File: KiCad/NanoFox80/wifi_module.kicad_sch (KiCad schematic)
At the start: 8 parts, among them U201 TPS22810DBVT, U202 74HC1G08

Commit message: Development
o Set all footprints to approximate values
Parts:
- C201: value 10uF -> (none); footprint Capacitors_SMD:C_0805 -> (none)
- C202: value 4.7uF -> (none); footprint Capacitors_SMD:C_0805 -> (none)
- C203: value 100nF -> (none); footprint Capacitors_SMD:C_0805 -> (none)
- MOD201: value HUZZAH_ESP8266_Breakout -> (none); footprint Oddities:Adafruit_HUZZAH_ESP8266_Breakout_SM -> (none)
- R201: value 560k -> (none); footprint Resistors_SMD:R_0805 -> (none)
- R202: value 10k -> (none); footprint Resistors_SMD:R_0805 -> (none)
- U201: value TPS22810DBVT -> (none); footprint TO_SOT_Packages_SMD:SOT-23-6 -> (none)
- U202: value 74HC1G08 -> (none); footprint TO_SOT_Packages_SMD:SOT-23-5 -> (none)
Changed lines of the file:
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@@
     (in_bom yes) (on_board yes)
     (property "Reference" "R202" (id 0) (at 220.98 99.822 90))
-    (property "Value" "10k" (id 1) (at 220.98 97.79 90))
-    (property "Footprint" "Resistors_SMD:R_0805" (id 2) (at 220.98 96.012 0)
+    (property "Value" "" (id 1) (at 220.98 97.79 90))
+    (property "Footprint" "" (id 2) (at 220.98 96.012 0)
       (effects (font (size 1.27 1.27)) hide)
     )
@@
       (effects (font (size 1.5494 1.5494) bold))
     )
-    (property "Value" "74HC1G08" (id 1) (at 135.89 110.49 0)
+    (property "Value" "" (id 1) (at 135.89 110.49 0)
       (effects (font (size 1.5494 1.5494) bold))
     )
-    (property "Footprint" "TO_SOT_Packages_SMD:SOT-23-5" (id 2) (at 134.62 109.22 0)
+    (property "Footprint" "" (id 2) (at 134.62 109.22 0)
       (effects (font (size 1.27 1.27)) hide)
     )
@@
       (effects (font (size 1.27 1.27)) (justify left))
     )
-    (property "Value" "4.7uF" (id 1) (at 247.015 88.9 0)
-      (effects (font (size 1.27 1.27)) (justify left))
-    )
-    (property "Footprint" "Capacitors_SMD:C_0805" (id 2) (at 247.3452 87.63 0)
+    (property "Value" "" (id 1) (at 247.015 88.9 0)
+      (effects (font (size 1.27 1.27)) (justify left))
+    )
+    (property "Footprint" "" (id 2) (at 247.3452 87.63 0)
       (effects (font (size 1.27 1.27)) hide)
     )
@@
       (effects (font (size 1.5494 1.5494) bold))
     )
-    (property "Value" "TPS22810DBVT" (id 1) (at 228.6 82.5759 0)
+    (property "Value" "" (id 1) (at 228.6 82.5759 0)
       (effects (font (size 1.5494 1.5494) bold))
     )
-    (property "Footprint" "TO_SOT_Packages_SMD:SOT-23-6" (id 2) (at 228.6 106.68 0)
+    (property "Footprint" "" (id 2) (at 228.6 106.68 0)
       (effects (font (size 1.27 1.27)) hide)
     )
@@
       (effects (font (size 1.27 1.27) bold))
     )
-    (property "Value" "HUZZAH_ESP8266_Breakout" (id 1) (at 177.8 109.22 0)
+    (property "Value" "" (id 1) (at 177.8 109.22 0)
       (effects (font (size 1.27 1.27) bold))
     )
-    (property "Footprint" "Oddities:Adafruit_HUZZAH_ESP8266_Breakout_SM" (id 2) (at 177.8 95.25 0)
+    (property "Footprint" "" (id 2) (at 177.8 95.25 0)
       (effects (font (size 1.27 1.27)) hide)
     )
@@
     (in_bom yes) (on_board yes)
     (property "Reference" "R201" (id 0) (at 117.602 95.25 90))
-    (property "Value" "560k" (id 1) (at 115.57 95.25 90))
-    (property "Footprint" "Resistors_SMD:R_0805" (id 2) (at 113.792 95.25 0)
+    (property "Value" "" (id 1) (at 115.57 95.25 90))
+    (property "Footprint" "" (id 2) (at 113.792 95.25 0)
       (effects (font (size 1.27 1.27)) hide)
     )
@@
       (effects (font (size 1.27 1.27)) (justify left))
     )
-    (property "Value" "10uF" (id 1) (at 210.185 88.9 0)
-      (effects (font (size 1.27 1.27)) (justify left))
-    )
-    (property "Footprint" "Capacitors_SMD:C_0805" (id 2) (at 210.5152 87.63 0)
+    (property "Value" "" (id 1) (at 210.185 88.9 0)
+      (effects (font (size 1.27 1.27)) (justify left))
+    )
+    (property "Footprint" "" (id 2) (at 210.5152 87.63 0)
       (effects (font (size 1.27 1.27)) hide)
     )
@@
       (effects (font (size 1.27 1.27)) (justify left))
     )
-    (property "Value" "100nF" (id 1) (at 137.16 102.87 90)
-      (effects (font (size 1.27 1.27)) (justify left))
-    )
-    (property "Footprint" "Capacitors_SMD:C_0805" (id 2) (at 134.62 100.33 0)
-      (effects (font (size 1.27 1.27)) hide)
-    )
+    (property "Value" "" (id 1) (at 137.16 102.87 90)
+      (effects (font (size 1.27 1.27)) (justify left))
+    )
+    (property "Footprint" "" (id 2) (at 134.62 100.33 0)
+      (effects (font (size 1.27 1.27)) hide)
+    )

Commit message: Development
o Updated version and date information
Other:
- title: (none) -> NanoFox80 Foxoring Transmitter
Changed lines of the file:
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@@
 (kicad_sch (version 20211123) (generator eeschema)
   (paper "A4")
+  (title_block
+    (title "NanoFox80 Foxoring Transmitter")
+    (date "2022-07-01")
+    (rev "0.4")
+  )
   (junction (at 209.55 86.36) (diameter 0) (color 0 0 0 0)
   )

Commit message: Development
o Changes to footprints in schematic
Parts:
- C201: value (none) -> 10uF; footprint (none) -> Capacitor_SMD:C_0805_2012Metric
- C202: value (none) -> 4.7uF; footprint (none) -> Capacitor_SMD:C_0805_2012Metric
- C203: value (none) -> 100nF; footprint (none) -> Capacitor_SMD:C_0805_2012Metric
- MOD201: value (none) -> HUZZAH_ESP8266_Breakout; footprint (none) -> Oddities:Adafruit_HUZZAH_ESP8266_Breakout_SM
- R201: value (none) -> 560k; footprint (none) -> Resistor_SMD:R_0805_2012Metric
- R202: value (none) -> 10k; footprint (none) -> Resistor_SMD:R_0805_2012Metric
- U201: value (none) -> TPS22810DBVT; footprint (none) -> Package_TO_SOT_SMD:SOT-23-6
- U202: value (none) -> 74HC1G08; footprint (none) -> Package_TO_SOT_SMD:SOT-23-5
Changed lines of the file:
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@@
     (in_bom yes) (on_board yes)
     (property "Reference" "R202" (id 0) (at 220.98 99.822 90))
-    (property "Value" "" (id 1) (at 220.98 97.79 90))
-    (property "Footprint" "" (id 2) (at 220.98 96.012 0)
+    (property "Value" "10k" (id 1) (at 220.98 97.79 90))
+    (property "Footprint" "Resistor_SMD:R_0805_2012Metric" (id 2) (at 220.98 96.012 0)
       (effects (font (size 1.27 1.27)) hide)
     )
@@
       (effects (font (size 1.5494 1.5494) bold))
     )
-    (property "Value" "" (id 1) (at 135.89 110.49 0)
+    (property "Value" "74HC1G08" (id 1) (at 135.89 110.49 0)
       (effects (font (size 1.5494 1.5494) bold))
     )
-    (property "Footprint" "" (id 2) (at 134.62 109.22 0)
+    (property "Footprint" "Package_TO_SOT_SMD:SOT-23-5" (id 2) (at 134.62 109.22 0)
       (effects (font (size 1.27 1.27)) hide)
     )
@@
       (effects (font (size 1.27 1.27)) (justify left))
     )
-    (property "Value" "" (id 1) (at 247.015 88.9 0)
-      (effects (font (size 1.27 1.27)) (justify left))
-    )
-    (property "Footprint" "" (id 2) (at 247.3452 87.63 0)
+    (property "Value" "4.7uF" (id 1) (at 247.015 88.9 0)
+      (effects (font (size 1.27 1.27)) (justify left))
+    )
+    (property "Footprint" "Capacitor_SMD:C_0805_2012Metric" (id 2) (at 247.3452 87.63 0)
       (effects (font (size 1.27 1.27)) hide)
     )
@@
       (effects (font (size 1.5494 1.5494) bold))
     )
-    (property "Value" "" (id 1) (at 228.6 82.5759 0)
+    (property "Value" "TPS22810DBVT" (id 1) (at 228.6 82.5759 0)
       (effects (font (size 1.5494 1.5494) bold))
     )
-    (property "Footprint" "" (id 2) (at 228.6 106.68 0)
+    (property "Footprint" "Package_TO_SOT_SMD:SOT-23-6" (id 2) (at 228.6 106.68 0)
       (effects (font (size 1.27 1.27)) hide)
     )
@@
       (effects (font (size 1.27 1.27) bold))
     )
-    (property "Value" "" (id 1) (at 177.8 109.22 0)
+    (property "Value" "HUZZAH_ESP8266_Breakout" (id 1) (at 177.8 109.22 0)
       (effects (font (size 1.27 1.27) bold))
     )
-    (property "Footprint" "" (id 2) (at 177.8 95.25 0)
+    (property "Footprint" "Oddities:Adafruit_HUZZAH_ESP8266_Breakout_SM" (id 2) (at 177.8 95.25 0)
       (effects (font (size 1.27 1.27)) hide)
     )
@@
     (in_bom yes) (on_board yes)
     (property "Reference" "R201" (id 0) (at 117.602 95.25 90))
-    (property "Value" "" (id 1) (at 115.57 95.25 90))
-    (property "Footprint" "" (id 2) (at 113.792 95.25 0)
+    (property "Value" "560k" (id 1) (at 115.57 95.25 90))
+    (property "Footprint" "Resistor_SMD:R_0805_2012Metric" (id 2) (at 113.792 95.25 0)
       (effects (font (size 1.27 1.27)) hide)
     )
@@
       (effects (font (size 1.27 1.27)) (justify left))
     )
-    (property "Value" "" (id 1) (at 210.185 88.9 0)
-      (effects (font (size 1.27 1.27)) (justify left))
-    )
-    (property "Footprint" "" (id 2) (at 210.5152 87.63 0)
+    (property "Value" "10uF" (id 1) (at 210.185 88.9 0)
+      (effects (font (size 1.27 1.27)) (justify left))
+    )
+    (property "Footprint" "Capacitor_SMD:C_0805_2012Metric" (id 2) (at 210.5152 87.63 0)
       (effects (font (size 1.27 1.27)) hide)
     )
@@
       (effects (font (size 1.27 1.27)) (justify left))
     )
-    (property "Value" "" (id 1) (at 137.16 102.87 90)
-      (effects (font (size 1.27 1.27)) (justify left))
-    )
-    (property "Footprint" "" (id 2) (at 134.62 100.33 0)
-      (effects (font (size 1.27 1.27)) hide)
-    )
+    (property "Value" "100nF" (id 1) (at 137.16 102.87 90)
+      (effects (font (size 1.27 1.27)) (justify left))
+    )
+    (property "Footprint" "Capacitor_SMD:C_0805_2012Metric" (id 2) (at 134.62 100.33 0)
+      (effects (font (size 1.27 1.27)) hide)
+    )

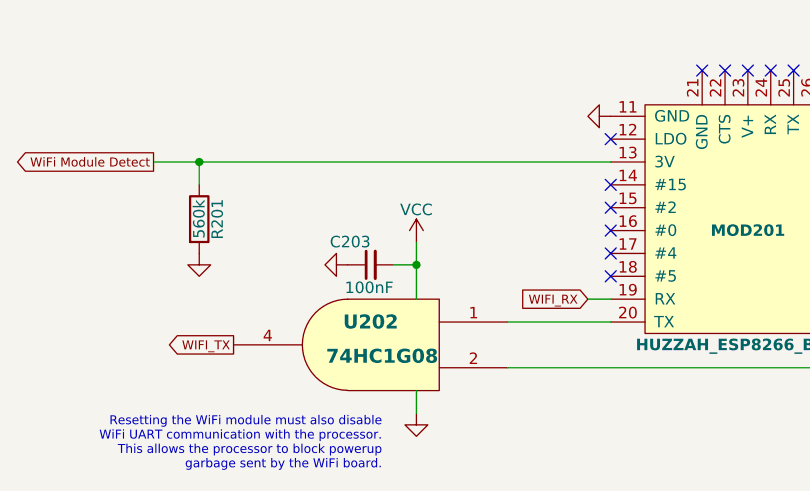
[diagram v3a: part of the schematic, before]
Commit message: Development
o Fixes to errors in schematic and PCB
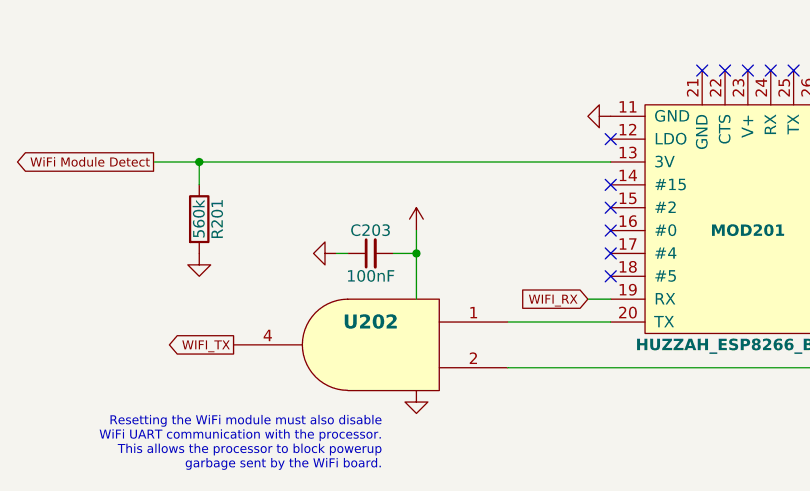
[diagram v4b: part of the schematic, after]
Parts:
- C203: footprint Capacitor_SMD:C_0805_2012Metric -> Capacitor_SMD:C_0805_2012Metric_Pad1.18x1.45mm_HandSolder; Digi-Key Part No. 478-1395-1-ND -> 445-5203-1-ND; LCSC Part Number C360619 -> (none); Link <a href="https://www.digikey.com/products/en?keywords=478-1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 -> (none); Manufacturer AVX Corporation -> TDK Corporation; Manufacturer PN 08055C104KAT2A -> C2012X7S2A474K125AB
- U202: value 74HC1G08 -> (none); footprint Package_TO_SOT_SMD:SOT-23-5 -> (none)
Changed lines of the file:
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@@
   (junction (at 228.6 97.79) (diameter 0) (color 0 0 0 0)
   )
+  (junction (at 139.7 99.06) (diameter 0) (color 0 0 0 0)
+  )
   (junction (at 217.17 97.79) (diameter 0) (color 0 0 0 0)
   )
@@
   )
   (junction (at 226.06 97.79) (diameter 0) (color 0 0 0 0)
-  )
-  (junction (at 139.7 100.33) (diameter 0) (color 0 0 0 0)
   )
   (no_connect (at 194.31 104.14))
@@
     (stroke (width 0) (type default) (color 0 0 0 0))
   )
-  (wire (pts (xy 139.7 116.84) (xy 139.7 114.3))
-    (stroke (width 0) (type default) (color 0 0 0 0))
-  )
   (wire (pts (xy 226.06 97.79) (xy 228.6 97.79))
     (stroke (width 0) (type default) (color 0 0 0 0))
@@
     (stroke (width 0) (type default) (color 0 0 0 0))
   )
-  (wire (pts (xy 161.29 88.9) (xy 115.57 88.9))
-    (stroke (width 0) (type default) (color 0 0 0 0))
-  )
   (wire (pts (xy 115.57 91.44) (xy 115.57 88.9))
     (stroke (width 0) (type default) (color 0 0 0 0))
   )
+  (wire (pts (xy 139.7 96.52) (xy 139.7 99.06))
+    (stroke (width 0) (type default) (color 0 0 0 0))
+  )
   (wire (pts (xy 218.44 88.9) (xy 217.17 88.9))
     (stroke (width 0) (type default) (color 0 0 0 0))
@@
     (stroke (width 0) (type default) (color 0 0 0 0))
   )
+  (wire (pts (xy 139.7 99.06) (xy 139.7 104.14))
+    (stroke (width 0) (type default) (color 0 0 0 0))
+  )
   (wire (pts (xy 231.14 93.98) (xy 231.14 97.79))
     (stroke (width 0) (type default) (color 0 0 0 0))
@@
     (stroke (width 0) (type default) (color 0 0 0 0))
   )
+  (wire (pts (xy 137.16 99.06) (xy 139.7 99.06))
+    (stroke (width 0) (type default) (color 0 0 0 0))
+  )
   (wire (pts (xy 217.17 88.9) (xy 217.17 97.79))
     (stroke (width 0) (type default) (color 0 0 0 0))
   )
+  (wire (pts (xy 132.08 99.06) (xy 130.81 99.06))
+    (stroke (width 0) (type default) (color 0 0 0 0))
+  )
   (wire (pts (xy 226.06 93.98) (xy 226.06 97.79))
     (stroke (width 0) (type default) (color 0 0 0 0))
@@
     (stroke (width 0) (type default) (color 0 0 0 0))
   )
+  (wire (pts (xy 115.57 88.9) (xy 161.29 88.9))
+    (stroke (width 0) (type default) (color 0 0 0 0))
+  )
   (wire (pts (xy 115.57 88.9) (xy 110.49 88.9))
     (stroke (width 0) (type default) (color 0 0 0 0))
@@
     (stroke (width 0) (type default) (color 0 0 0 0))
   )
-  (wire (pts (xy 139.7 97.79) (xy 139.7 100.33))
+  (wire (pts (xy 194.31 86.36) (xy 209.55 86.36))
     (stroke (width 0) (type default) (color 0 0 0 0))
   )
@@
     (stroke (width 0) (type default) (color 0 0 0 0))
   )
-  (wire (pts (xy 139.7 100.33) (xy 139.7 104.14))
-    (stroke (width 0) (type default) (color 0 0 0 0))
-  )
-  (wire (pts (xy 194.31 86.36) (xy 209.55 86.36))
-    (stroke (width 0) (type default) (color 0 0 0 0))
-  )
   (wire (pts (xy 209.55 86.36) (xy 218.44 86.36))
-    (stroke (width 0) (type default) (color 0 0 0 0))
-  )
-  (wire (pts (xy 137.16 100.33) (xy 139.7 100.33))
     (stroke (width 0) (type default) (color 0 0 0 0))
   )
@@
     )
     (property "Datasheet" "" (id 3) (at 161.29 83.82 0)
+      (effects (font (size 1.27 1.27)) hide)
+    )
+    (pin "1")
+  )
+  (symbol (lib_id "power:GND") (at 130.81 99.06 270) (unit 1)
+    (in_bom yes) (on_board yes) (fields_autoplaced)
+    (property "Reference" "#PWR0208" (id 0) (at 124.46 99.06 0)
+      (effects (font (size 1.27 1.27)) hide)
+    )
+    (property "Value" "GND" (id 1) (at 126.3666 99.06 0)
+      (effects (font (size 1.27 1.27)) hide)
+    )
+    (property "Footprint" "" (id 2) (at 130.81 99.06 0)
+      (effects (font (size 1.27 1.27)) hide)
+    )
+    (property "Datasheet" "" (id 3) (at 130.81 99.06 0)
       (effects (font (size 1.27 1.27)) hide)
     )
@@
       (effects (font (size 1.5494 1.5494) bold))
     )
-    (property "Value" "74HC1G08" (id 1) (at 135.89 110.49 0)
+    (property "Value" "" (id 1) (at 135.89 110.49 0)
       (effects (font (size 1.5494 1.5494) bold))
     )
-    (property "Footprint" "Package_TO_SOT_SMD:SOT-23-5" (id 2) (at 134.62 109.22 0)
+    (property "Footprint" "" (id 2) (at 134.62 109.22 0)
       (effects (font (size 1.27 1.27)) hide)
     )
@@
     (pin "2")
     (pin "4")
+  )
+  (symbol (lib_id "Device:C_Small") (at 134.62 99.06 90) (unit 1)
+    (in_bom yes) (on_board yes)
+    (property "Reference" "C203" (id 0) (at 134.62 96.52 90))
+    (property "Value" "100nF" (id 1) (at 134.62 101.6 90))
+    (property "Footprint" "Capacitor_SMD:C_0805_2012Metric_Pad1.18x1.45mm_HandSolder" (id 2) (at 134.62 99.06 0)
+      (effects (font (size 1.27 1.27)) hide)
+    )
+    (property "Datasheet" "~" (id 3) (at 134.62 99.06 0)
+      (effects (font (size 1.27 1.27)) hide)
+    )
+    (property "Digi-Key Part No." "445-5203-1-ND" (id 4) (at 134.62 99.06 0)
+      (effects (font (size 1.27 1.27)) hide)
+    )
+    (property "Manufacturer" "TDK Corporation" (id 5) (at 134.62 99.06 0)
+      (effects (font (size 1.27 1.27)) hide)
+    )
+    (property "Manufacturer PN" "C2012X7S2A474K125AB" (id 6) (at 134.62 99.06 0)
+      (effects (font (size 1.27 1.27)) hide)
+    )
+    (property "Description" "CAP CER 0.47UF 100V X7S 0805" (id 7) (at 134.62 99.06 0)
+      (effects (font (size 1.27 1.27)) hide)
+    )
+    (pin "1")
+    (pin "2")
   )
   (symbol (lib_id "Device:C") (at 246.38 91.44 0) (mirror x) (unit 1)
@@
     (pin "1")
   )
-  (symbol (lib_id "power:GND") (at 132.08 100.33 270) (unit 1)
-    (in_bom yes) (on_board yes) (fields_autoplaced)
-    (property "Reference" "#PWR0208" (id 0) (at 125.73 100.33 0)
-      (effects (font (size 1.27 1.27)) hide)
-    )
-    (property "Value" "GND" (id 1) (at 127.6366 100.33 0)
-      (effects (font (size 1.27 1.27)) hide)
-    )
-    (property "Footprint" "" (id 2) (at 132.08 100.33 0)
-      (effects (font (size 1.27 1.27)) hide)
-    )
-    (property "Datasheet" "" (id 3) (at 132.08 100.33 0)
-      (effects (font (size 1.27 1.27)) hide)
-    )
-    (pin "1")
-  )
   (symbol (lib_id "power:GND") (at 246.38 95.25 0) (unit 1)
     (in_bom yes) (on_board yes) (fields_autoplaced)
@@
     (pin "5")
     (pin "6")
+  )
+  (symbol (lib_id "power:GND") (at 139.7 114.3 0) (unit 1)
+    (in_bom yes) (on_board yes) (fields_autoplaced)
+    (property "Reference" "#PWR0151" (id 0) (at 139.7 120.65 0)
+      (effects (font (size 1.27 1.27)) hide)
+    )
+    (property "Value" "GND" (id 1) (at 139.7 118.7434 0)
+      (effects (font (size 1.27 1.27)) hide)
+    )
+    (property "Footprint" "" (id 2) (at 139.7 114.3 0)
+      (effects (font (size 1.27 1.27)) hide)
+    )
+    (property "Datasheet" "" (id 3) (at 139.7 114.3 0)
+      (effects (font (size 1.27 1.27)) hide)
+    )
+    (pin "1")
   )
   (symbol (lib_id "MCU_Espressif:HUZZAH_ESP8266_Breakout") (at 177.8 95.25 180) (unit 1)
@@
     (pin "2")
   )
-  (symbol (lib_id "power:VCC") (at 139.7 97.79 0) (unit 1)
-    (in_bom yes) (on_board yes) (fields_autoplaced)
-    (property "Reference" "#PWR0206" (id 0) (at 139.7 101.6 0)
-      (effects (font (size 1.27 1.27)) hide)
-    )
-    (property "Value" "VCC" (id 1) (at 139.7 94.2142 0))
-    (property "Footprint" "" (id 2) (at 139.7 97.79 0)
-      (effects (font (size 1.27 1.27)) hide)
-    )
-    (property "Datasheet" "" (id 3) (at 139.7 97.79 0)
+  (symbol (lib_id "power:VDD") (at 139.7 96.52 0) (unit 1)
+    (in_bom yes) (on_board yes) (fields_autoplaced)
+    (property "Reference" "#PWR0150" (id 0) (at 139.7 100.33 0)
+      (effects (font (size 1.27 1.27)) hide)
+    )
+    (property "Value" "" (id 1) (at 139.7 92.9442 0))
+    (property "Footprint" "" (id 2) (at 139.7 96.52 0)
+      (effects (font (size 1.27 1.27)) hide)
+    )
+    (property "Datasheet" "" (id 3) (at 139.7 96.52 0)
       (effects (font (size 1.27 1.27)) hide)
     )
@@
     (pin "2")
   )
-  (symbol (lib_id "Device:C_Small") (at 134.62 100.33 90) (mirror x) (unit 1)
-    (in_bom yes) (on_board yes)
-    (property "Reference" "C203" (id 0) (at 134.62 97.79 90)
-      (effects (font (size 1.27 1.27)) (justify left))
-    )
-    (property "Value" "100nF" (id 1) (at 137.16 102.87 90)
-      (effects (font (size 1.27 1.27)) (justify left))
-    )
-    (property "Footprint" "Capacitor_SMD:C_0805_2012Metric" (id 2) (at 134.62 100.33 0)
-      (effects (font (size 1.27 1.27)) hide)
-    )
-    (property "Datasheet" "" (id 3) (at 134.62 100.33 0)
-      (effects (font (size 1.27 1.27)) hide)
-    )
-    (property "Digi-Key Part No." "478-1395-1-ND" (id 4) (at 134.62 100.33 0)
-      (effects (font (size 1.27 1.27)) hide)
-    )
-    (property "Link" "<a href=\"https://www.digikey.com/products/en?keywords=478-1395-1-ND\">Link</a>" (id 5) (at 134.62 100.33 0)
-      (effects (font (size 1.524 1.524)) hide)
-    )
-    (property "Manufacturer" "AVX Corporation" (id 6) (at 134.62 100.33 0)
-      (effects (font (size 1.27 1.27)) hide)
-    )
-    (property "Manufacturer PN" "08055C104KAT2A" (id 7) (at 134.62 100.33 0)
-      (effects (font (size 1.27 1.27)) hide)
-    )
-    (property "Description" "CAP CER 0.1UF 50V X7R 0805" (id 8) (at 134.62 100.33 0)
-      (effects (font (size 1.27 1.27)) hide)
-    )
-    (property "LCSC Part Number" "C360619" (id 9) (at 134.62 100.33 0)
-      (effects (font (size 1.27 1.27)) hide)
-    )
-    (pin "1")
-    (pin "2")
-  )
   (symbol (lib_id "power:GND") (at 194.31 83.82 90) (unit 1)
     (in_bom yes) (on_board yes) (fields_autoplaced)
@@
       (effects (font (size 1.27 1.27)) hide)
     )
-    (pin "1")
-  )
-  (symbol (lib_id "power:GND") (at 139.7 116.84 0) (unit 1)
-    (in_bom yes) (on_board yes) (fields_autoplaced)
-    (property "Reference" "#PWR0210" (id 0) (at 139.7 123.19 0)
-      (effects (font (size 1.27 1.27)) hide)
-    )
-    (property "Value" "GND" (id 1) (at 139.7 121.2834 0)
-      (effects (font (size 1.27 1.27)) hide)
-    )
-    (property "Footprint" "" (id 2) (at 139.7 116.84 0)
-      (effects (font (size 1.27 1.27)) hide)
-    )
-    (property "Datasheet" "" (id 3) (at 139.7 116.84 0)
-      (effects (font (size 1.27 1.27)) hide)
-    )

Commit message: Development
PCB Changes
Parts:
- U202: value (none) -> 74HC1G08; footprint (none) -> Package_TO_SOT_SMD:SOT-23-5
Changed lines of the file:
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@@
       (effects (font (size 1.5494 1.5494) bold))
     )
-    (property "Value" "" (id 1) (at 135.89 110.49 0)
-      (effects (font (size 1.5494 1.5494) bold))
-    )
-    (property "Footprint" "" (id 2) (at 134.62 109.22 0)
+    (property "Value" "74HC1G08" (id 1) (at 135.89 110.49 0)
+      (effects (font (size 1.5494 1.5494) bold))
+    )
+    (property "Footprint" "Package_TO_SOT_SMD:SOT-23-5" (id 2) (at 134.62 109.22 0)
       (effects (font (size 1.27 1.27)) hide)
     )
@@
       (effects (font (size 1.27 1.27)) hide)
     )
-    (property "Value" "" (id 1) (at 139.7 92.9442 0))
+    (property "Value" "VDD" (id 1) (at 139.7 92.9442 0))
     (property "Footprint" "" (id 2) (at 139.7 96.52 0)
       (effects (font (size 1.27 1.27)) hide)
